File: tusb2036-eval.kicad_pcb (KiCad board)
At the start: 2 copper layers, 85 x 52 mm, 48 parts, among them J1 USB_B_Micro, J2 USB_A, J3 USB_A, J4 USB_A, SW1 RESET, U1 TUSB2036, U2 TPS76333, U3 TPS2044D, U4 SN75240, U5 SN75240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

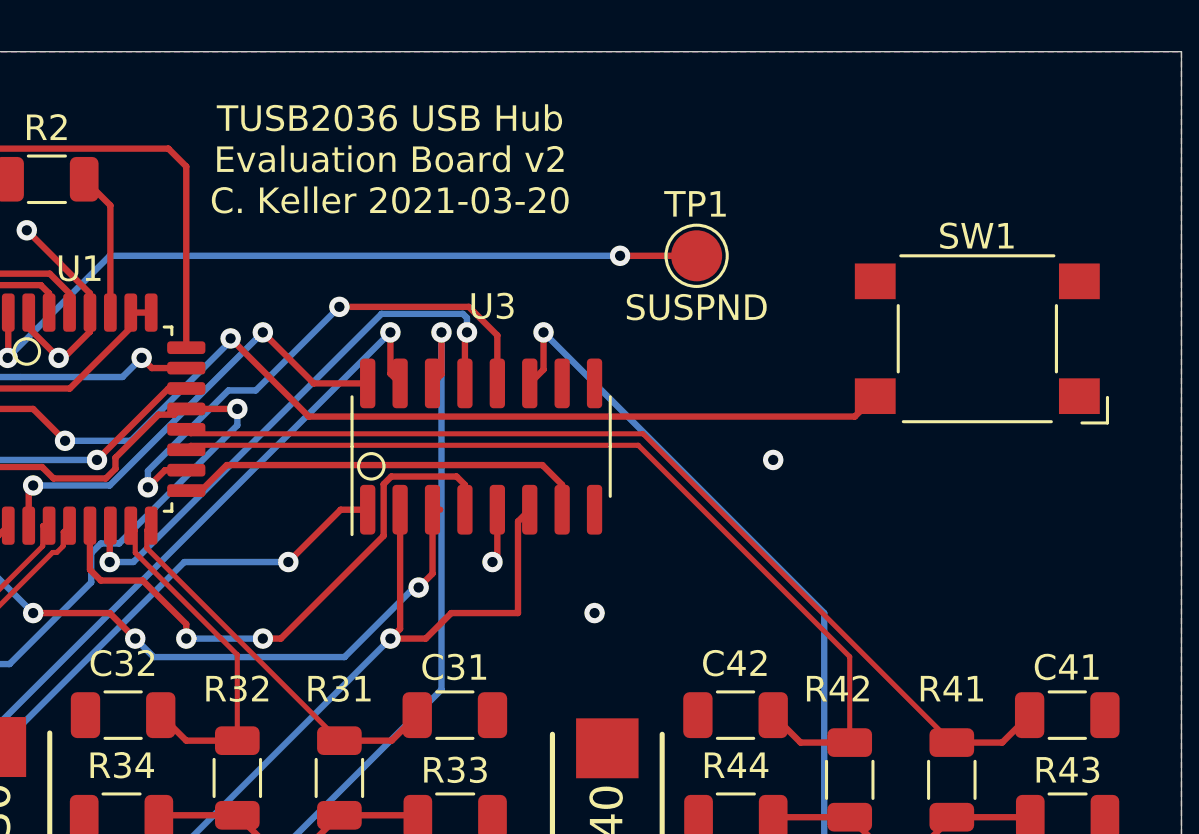
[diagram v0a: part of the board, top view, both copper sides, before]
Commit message: Add R3 to disable TPS2044 OUT4
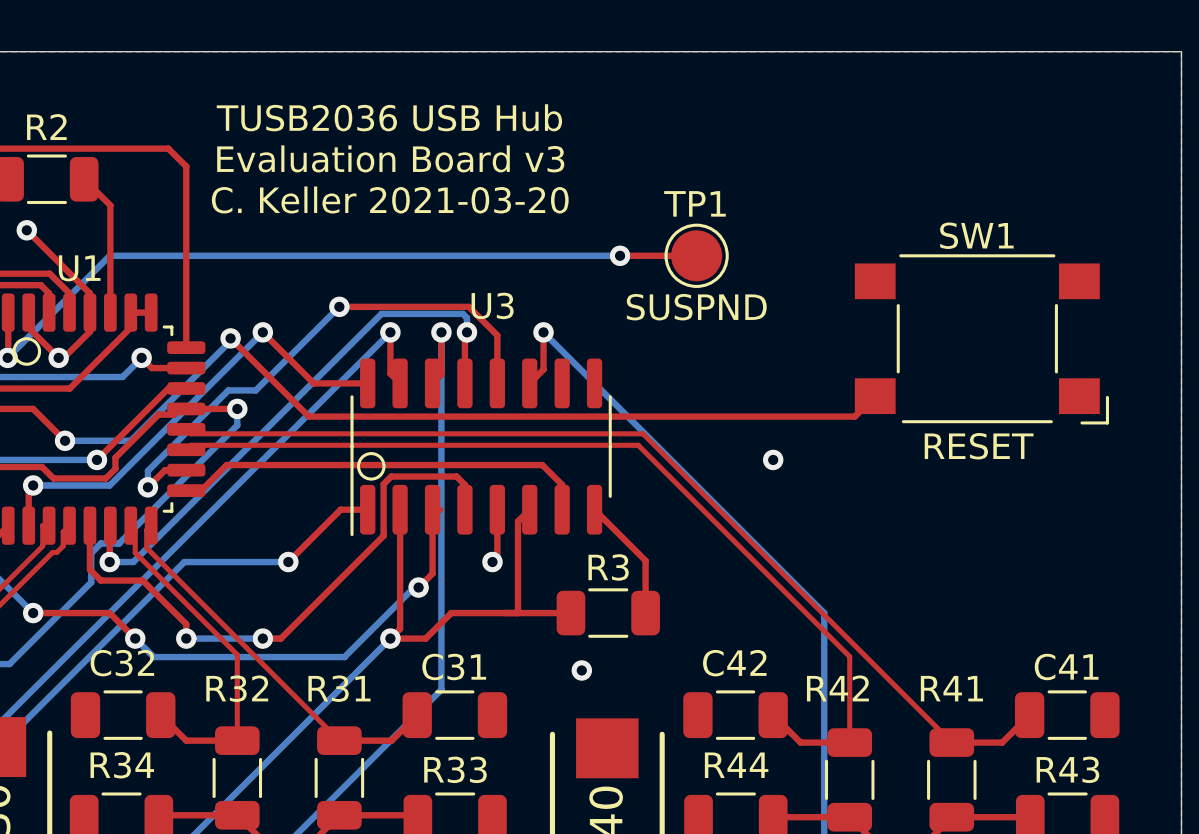
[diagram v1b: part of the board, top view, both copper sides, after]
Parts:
- added R3: 15kΩ, Resistor_SMD:R_1206_3216Metric, F.Cu at (159.3, 95.2)
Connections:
- U3 pad 8: (no net) -> Net-(R3-Pad1)
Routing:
- net Net-(R3-Pad1): track 0.00 -> 4.88 mm
- net VBUS: track 123.8 -> 126.4 mm
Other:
- board text added: "TUSB2036 USB Hub Evaluation Board v3 C. Keller 2021-03-20"
- board text removed: "TUSB2036 USB Hub Evaluation Board v2 C. Keller 2021-03-20"
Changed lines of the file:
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@@
     (thickness 1.6)
     (drawings 16)
-    (tracks 473)
+    (tracks 477)
     (zones 0)
-    (modules 48)
-    (nets 40)
+    (modules 49)
+    (nets 41)
   )
   (page A4)
@@
     (title "TUSB2036 Evaluation Board")
     (date 2021-03-20)
-    (rev 2)
+    (rev 3)
     (company "Chris Keller")
   )
@@
   (net 38 /EN1)
   (net 39 "Net-(R2-Pad1)")
+  (net 40 "Net-(R3-Pad1)")
   (net_class Default "This is the default net class."
     (clearance 0.2)
@@
     (add_net "Net-(J1-Pad2)")
     (add_net "Net-(J1-Pad3)")
-    (add_net "Net-(J1-Pad4)")
     (add_net "Net-(J1-Pad6)")
     (add_net "Net-(J2-Pad2)")
     (add_net "Net-(J2-Pad3)")
-    (add_net "Net-(J2-Pad5)")
     (add_net "Net-(J3-Pad2)")
     (add_net "Net-(J3-Pad3)")
-    (add_net "Net-(J3-Pad5)")
     (add_net "Net-(J4-Pad2)")
     (add_net "Net-(J4-Pad3)")
-    (add_net "Net-(J4-Pad5)")
     (add_net "Net-(R2-Pad1)")
+    (add_net "Net-(R3-Pad1)")
     (add_net "Net-(SW1-Pad2)")
     (add_net "Net-(TP1-Pad1)")
-    (add_net "Net-(U1-Pad5)")
-    (add_net "Net-(U2-Pad4)")
-    (add_net "Net-(U3-Pad10)")
-    (add_net "Net-(U3-Pad8)")
-    (add_net "Net-(U3-Pad9)")
     (add_net VBUS)
+  )
+  (module Resistor_SMD:R_1206_3216Metric (layer F.Cu)
+    (at 159.2875 95.25 180)
+    (descr "Resistor SMD 1206 (3216 Metric), square (rectangular) end terminal, IPC_7351 nominal, (Body size source: IPC-SM-782 page 72, https://www.pcb-3d.com/wordpress/wp-content/uploads/ipc-sm-782a_amendment_1_and_2.pdf), generated with kicad-footprint-generator")
+    (tags resistor)
+    (attr smd)
+    (fp_text reference R3 (at 0 1.75) (layer F.SilkS)
+      (effects (font (size 1 1) (thickness 0.15)))
+    )
+    (fp_text value 15kΩ (at 0 1.82) (layer F.Fab)
+      (effects (font (size 1 1) (thickness 0.15)))
+    )
+    (fp_line (start 2.28 1.12) (end -2.28 1.12) (layer F.CrtYd) (width 0.05))
+    (fp_line (start 2.28 -1.12) (end 2.28 1.12) (layer F.CrtYd) (width 0.05))
+    (fp_line (start -2.28 -1.12) (end 2.28 -1.12) (layer F.CrtYd) (width 0.05))
+    (fp_line (start -2.28 1.12) (end -2.28 -1.12) (layer F.CrtYd) (width 0.05))
+    (fp_line (start -0.727064 0.91) (end 0.727064 0.91) (layer F.SilkS) (width 0.12))
+    (fp_line (start -0.727064 -0.91) (end 0.727064 -0.91) (layer F.SilkS) (width 0.12))
+    (fp_line (start 1.6 0.8) (end -1.6 0.8) (layer F.Fab) (width 0.1))
+    (fp_line (start 1.6 -0.8) (end 1.6 0.8) (layer F.Fab) (width 0.1))
+    (fp_line (start -1.6 -0.8) (end 1.6 -0.8) (layer F.Fab) (width 0.1))
+    (fp_line (start -1.6 0.8) (end -1.6 -0.8) (layer F.Fab) (width 0.1))
+    (fp_text user %R (at 0 0) (layer F.Fab)
+      (effects (font (size 0.8 0.8) (thickness 0.12)))
+    )
+    (pad 2 smd roundrect (at 1.4625 0 180) (size 1.125 1.75) (layers F.Cu F.Paste F.Mask) (roundrect_rratio 0.222222)
+      (net 6 VBUS))
+    (pad 1 smd roundrect (at -1.4625 0 180) (size 1.125 1.75) (layers F.Cu F.Paste F.Mask) (roundrect_rratio 0.222222)
+      (net 40 "Net-(R3-Pad1)"))
+    (model ${KISYS3DMOD}/Resistor_SMD.3dshapes/R_1206_3216Metric.wrl
+      (at (xyz 0 0 0))
+      (scale (xyz 1 1 1))
+      (rotate (xyz 0 0 0))
+    )
   )
   (module Vishay-cap:CAPPM7343X310N locked (layer F.Cu)
@@
     (pad 10 smd roundrect (at 2.475 3.175 90) (size 1.95 0.6) (layers F.Cu F.Paste F.Mask) (roundrect_rratio 0.25))
     (pad 9 smd roundrect (at 2.475 4.445 90) (size 1.95 0.6) (layers F.Cu F.Paste F.Mask) (roundrect_rratio 0.25))
-    (pad 8 smd roundrect (at -2.475 4.445 90) (size 1.95 0.6) (layers F.Cu F.Paste F.Mask) (roundrect_rratio 0.25))
+    (pad 8 smd roundrect (at -2.475 4.445 90) (size 1.95 0.6) (layers F.Cu F.Paste F.Mask) (roundrect_rratio 0.25)
+      (net 40 "Net-(R3-Pad1)"))
     (pad 7 smd roundrect (at -2.475 3.175 90) (size 1.95 0.6) (layers F.Cu F.Paste F.Mask) (roundrect_rratio 0.25)
       (net 34 /EN3))
@@
       (effects (font (size 1 1) (thickness 0.15)))
     )
-    (fp_text value RESET (at 0 4.2) (layer F.Fab)
+    (fp_text value RESET (at 0 -4.25) (layer F.SilkS)
       (effects (font (size 1 1) (thickness 0.15)))
     )
@@
   (gr_circle (center 150 89.5) (end 150.5 89.5) (layer F.SilkS) (width 0.12))
   (gr_circle (center 136.5 85) (end 137 85) (layer F.SilkS) (width 0.12))
-  (gr_text "TUSB2036 USB Hub\nEvaluation Board v2\nC. Keller 2021-03-20" (at 150.75 77.5) (layer F.SilkS)
+  (gr_text "TUSB2036 USB Hub\nEvaluation Board v3\nC. Keller 2021-03-20" (at 150.75 77.5) (layer F.SilkS)
     (effects (font (size 1 1) (thickness 0.15)))
   )
@@
   (via (at 118.75 83.25) (size 0.8) (drill 0.4) (layers F.Cu B.Cu) (net 1))
   (via (at 146.75 93.25) (size 0.8) (drill 0.4) (layers F.Cu B.Cu) (net 1))
-  (via (at 158.75 95.25) (size 0.8) (drill 0.4) (layers F.Cu B.Cu) (net 1))
+  (via (at 158.25 97.5) (size 0.8) (drill 0.4) (layers F.Cu B.Cu) (net 1))
   (via (at 165.75 89.25) (size 0.8) (drill 0.4) (layers F.Cu B.Cu) (net 1))
   (segment (start 148.8 91.2) (end 146.75 93.25) (width 0.25) (layer F.Cu) (net 1))
@@
   (segment (start 152.135 96.25) (end 153.135 95.25) (width 0.25) (layer F.Cu) (net 6))
   (segment (start 150.75 96.25) (end 152.135 96.25) (width 0.25) (layer F.Cu) (net 6))
-  (segment (start 153.135 95.25) (end 155.75 95.25) (width 0.25) (layer F.Cu) (net 6))
   (segment (start 155.75 91.66) (end 156.21 91.2) (width 0.25) (layer F.Cu) (net 6))
   (segment (start 155.75 95.25) (end 155.75 91.66) (width 0.25) (layer F.Cu) (net 6))
@@
   (segment (start 104.43 87.2) (end 104.505001 87.124999) (width 0.25) (layer F.Cu) (net 6))
   (segment (start 103.65 87.2) (end 104.43 87.2) (width 0.25) (layer F.Cu) (net 6))
+  (segment (start 157.825 95.25) (end 155.25 95.25) (width 0.25) (layer F.Cu) (net 6))
+  (segment (start 155.25 95.25) (end 155.75 95.25) (width 0.25) (layer F.Cu) (net 6))
+  (segment (start 153.135 95.25) (end 155.25 95.25) (width 0.25) (layer F.Cu) (net 6))
   (segment (start 133.65 86.45) (end 134.4 86.45) (width 0.25) (layer F.Cu) (net 7))
   (segment (start 132.753767 87.346233) (end 133.65 86.45) (width 0.25) (layer F.Cu) (net 7))
@@
   (segment (start 139.775 79.275) (end 139.775 83.475) (width 0.25) (layer F.Cu) (net 39))
   (segment (start 138.75 78.25) (end 139.775 79.275) (width 0.25) (layer F.Cu) (net 39))
+  (segment (start 160.75 93.2) (end 158.75 91.2) (width 0.25) (layer F.Cu) (net 40))
+  (segment (start 160.75 95.25) (end 160.75 93.2) (width 0.25) (layer F.Cu) (net 40))
   (zone (net 1) (net_name GND) (layer F.Cu) (hatch edge 0.508)
     (connect_pads (clearance 0.508))

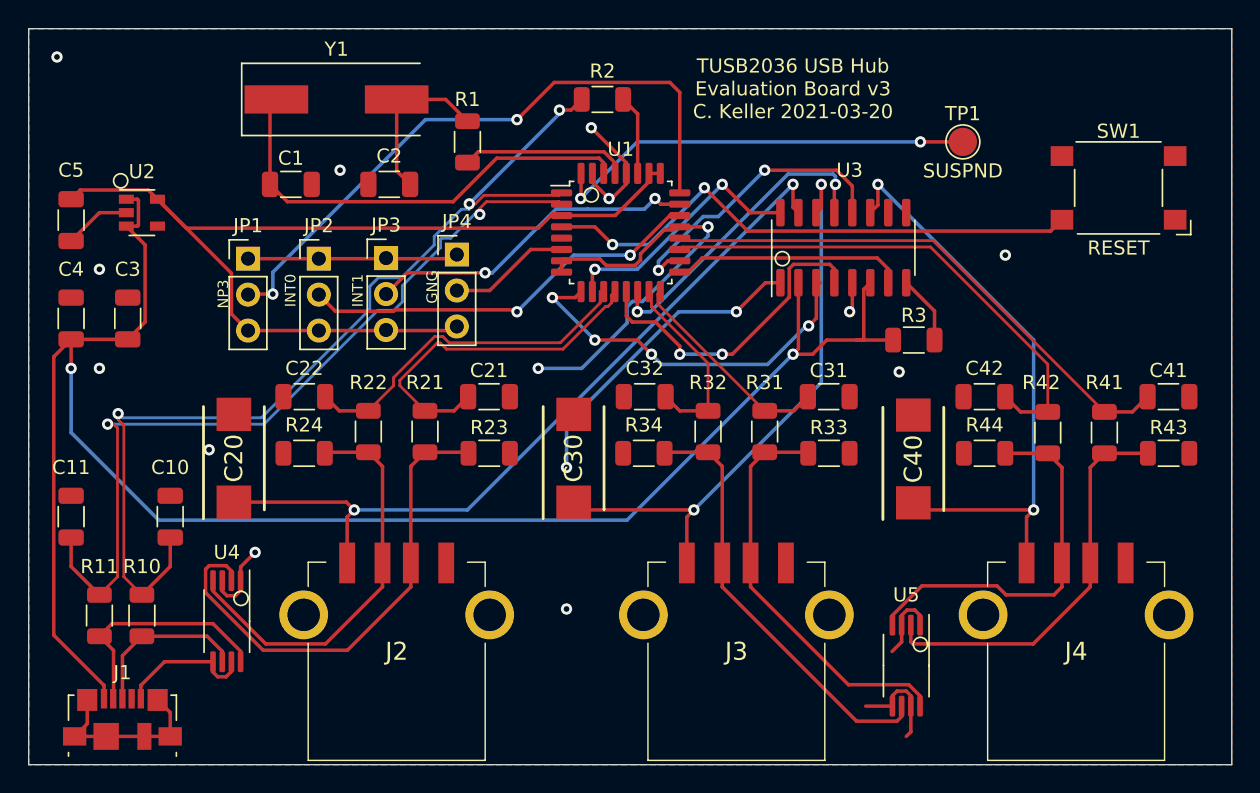
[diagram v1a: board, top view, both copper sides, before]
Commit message: Thicker power traces and fix 3D models
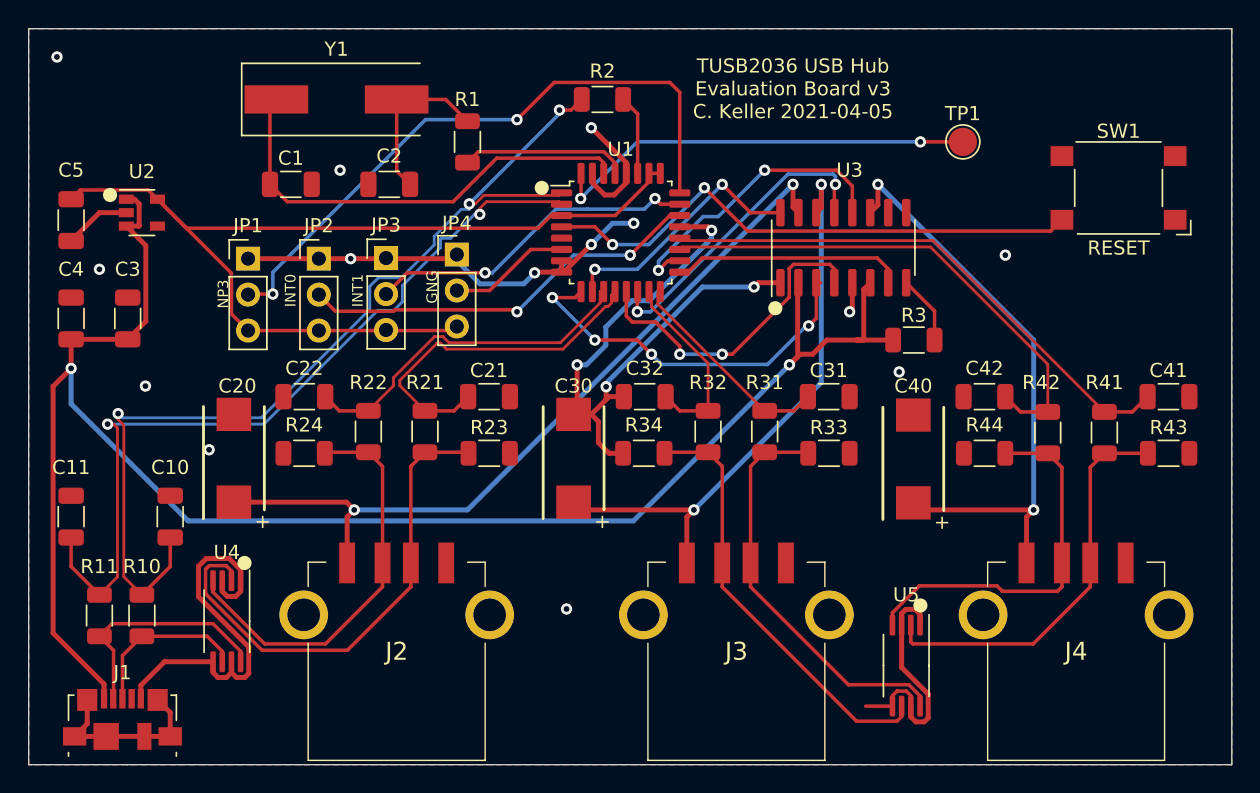
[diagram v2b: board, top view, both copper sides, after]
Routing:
- net GND: track 111.3 -> 138.2 mm, vias 16 -> 18
- net VBUS: track 126.4 -> 124.1 mm
- net Net-(J2-Pad2): track 28.3 -> 29.0 mm
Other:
- net class Power added: clearance 0.2, trace_width 0.35, via_dia 0.8, via_drill 0.4
- board text added: "TUSB2036 USB Hub Evaluation Board v3 C. Keller 2021-04-05"
- board text removed: "TUSB2036 USB Hub Evaluation Board v3 C. Keller 2021-03-20"
